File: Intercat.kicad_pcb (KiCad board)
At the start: 2 copper layers, 74.9 x 37.5 mm, 81 parts, among them J1 Conn_01x02, J2 Conn_01x02, J3 DE9_Receptacle, J4 USB_C_Receptacle_USB2.0, J5 Conn_01x02, T1 LM-NP-1001-B1L, T4 LM-NP-1001-B1L, U1 CP2615-xx-xM, U10 MAX3250, U11 EL357N(C)(TA)-G, U12 EL357N(C)(TA)-G, U2 USBLC6-2SC6, U3 PCM3060, U4 MCP6002, U6 MCP6002, U8 EL357N(C)(TA)-G, U9 EL357N(C)(TA)-G

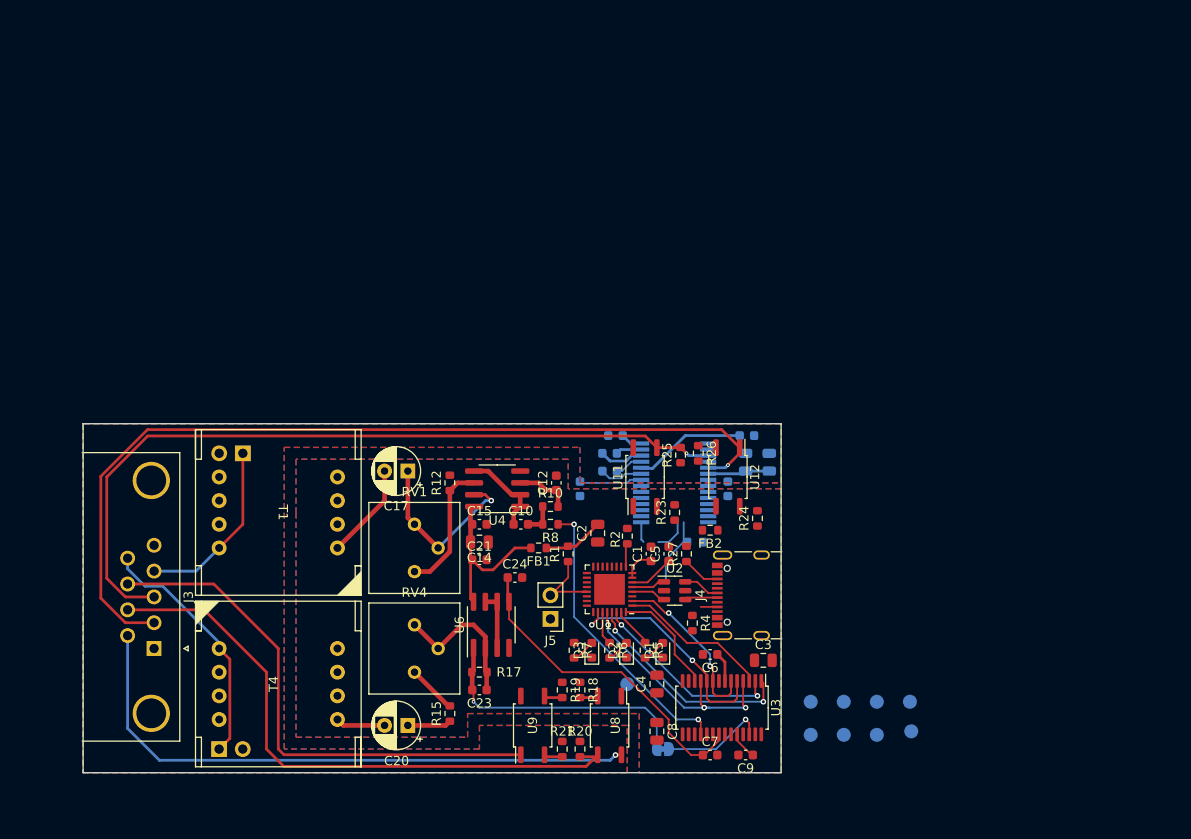
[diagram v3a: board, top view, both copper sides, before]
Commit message: redone layout, reduced size, added clearance for box
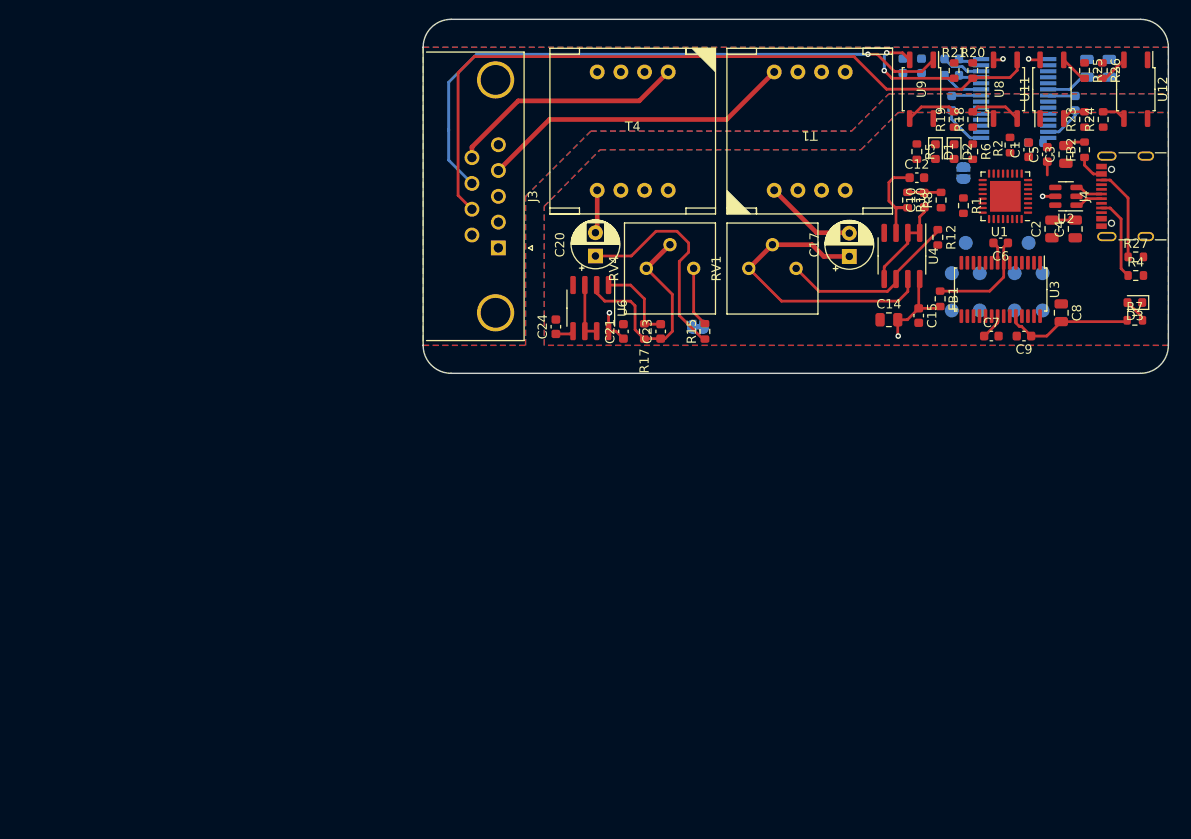
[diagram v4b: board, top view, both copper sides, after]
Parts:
- removed J1, J2, J5: Conn_01x02, Connector_PinHeader_2.54mm:PinHeader_1x02_P2.54mm_Vertical
- added JP1: Jumper_2_Open, Jumper:SolderJumper-2_P1.3mm_Open_RoundedPad1.0x1.5mm, B.Cu at (158.0, 78.5)
- added TP9: TestPoint, TestPoint:TestPoint_Pad_D1.5mm, B.Cu at (156.8, 93.2)
- moved R20 84.2 mm to (159.0, 67.5)
- moved R21 84.1 mm to (157.0, 67.5)
- moved U8 80.4 mm to (162.5, 69.5), turned to 90 degrees
- moved U9 80.0 mm to (153.5, 69.5), turned to -90 degrees
- moved R18 74.3 mm to (159.0, 72.8), turned to 90 degrees
- moved R19 74.3 mm to (157.0, 72.8), turned to 90 degrees
- moved T4 70.5 mm to (122.5, 74.0), turned to 0 degrees
- moved T1 70.2 mm to (141.5, 74.0), turned to 180 degrees
- moved R7 69.8 mm to (176.4, 94.3), turned to 0 degrees
- moved D3 69.2 mm to (176.4, 92.4), turned to 180 degrees
- moved C4 66.4 mm to (170.0, 84.5)
- moved R6 66.2 mm to (159.0, 76.2)
- moved D2 64.0 mm to (157.0, 76.2), turned to -90 degrees
- moved C3 63.3 mm to (169.0, 76.5), turned to 90 degrees
- moved C8 62.5 mm to (168.5, 93.5)
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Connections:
- U2 pad 1: /D- -> /D+
- U2 pad 3: /D+ -> /D-
- U2 pad 4: /D+ -> /D-
- U2 pad 6: /D- -> /D+
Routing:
- net /RX_ISO: track 96.0 -> 0.00 mm, vias 1 -> 0
- net /TX_ISO: track 84.1 -> 3.05 mm, vias 1 -> 0
- net VS: track 64.6 -> 2.33 mm, vias 1 -> 2
- net /DAC_Rout: track 31.3 -> 0.00 mm, vias 2 -> 0
- net /DAC_Vref: track 35.2 -> 4.73 mm
- net /LRCLK: track 26.9 -> 0.00 mm, vias 3 -> 0
- net /MCLK: track 24.8 -> 0.00 mm, vias 2 -> 0
- net /SCL: track 23.5 -> 0.00 mm, vias 2 -> 0
- net /SDA: track 21.0 -> 0.00 mm, vias 2 -> 0
- net Net-(JP2-A): track 29.6 -> 8.90 mm, vias 1 -> 0
- net Net-(C20-Pad1): track 4.69 -> 23.6 mm
- net /SCLK: track 18.5 -> 0.00 mm, vias 2 -> 0
- net /DIN: track 16.3 -> 0.00 mm
- net /OUT_ISO: track 19.2 -> 34.0 mm
- net /RTS_ISO: track 64.8 -> 79.4 mm
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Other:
- board size 74.9 x 37.5 mm -> 80 x 38 mm

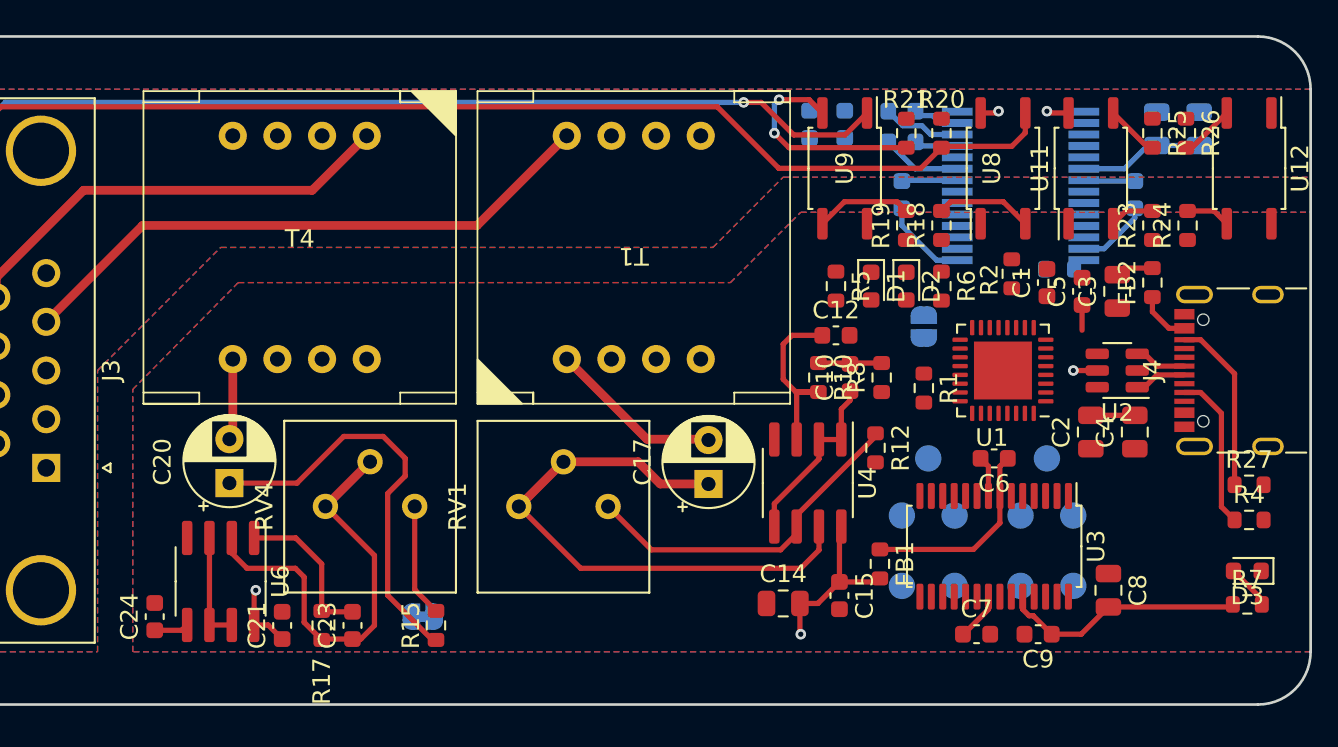
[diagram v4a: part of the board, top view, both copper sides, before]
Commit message: removed missed cap,reviewed layout
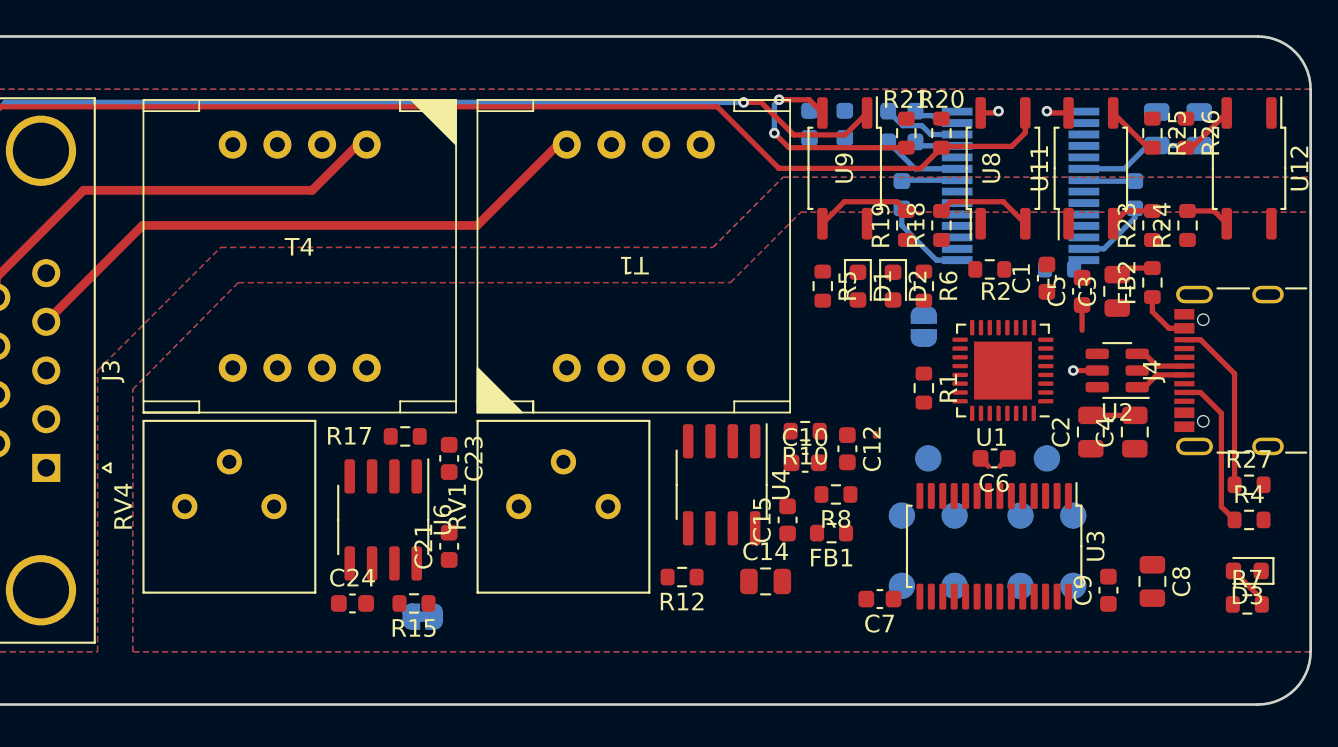
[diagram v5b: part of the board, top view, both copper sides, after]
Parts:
- removed C17, C20: C_Polarized, Capacitor_THT:CP_Radial_D5.0mm_P2.50mm
- R15: value 3k9 -> 9k1
- moved R12 13.2 mm to (144.2, 92.8), turned to 180 degrees
- moved R17 11.8 mm to (128.5, 84.8), turned to 0 degrees
- moved C24 11.3 mm to (125.5, 94.2), turned to 0 degrees
- moved C23 11.0 mm to (131.0, 86.0), turned to -90 degrees
- moved C21 10.5 mm to (131.0, 91.0)
- moved U6 9.89 mm to (127.2, 89.5)
- moved RV4 8.00 mm to (121.0, 88.7)
- moved R8 7.14 mm to (153.0, 88.0), turned to 180 degrees
- moved C12 6.48 mm to (153.7, 85.5), turned to -90 degrees
- moved C7 5.85 mm to (155.5, 94.0), turned to 180 degrees
- moved C10 5.48 mm to (151.2, 86.2), turned to 0 degrees
- moved C15 5.21 mm to (150.2, 89.5), turned to 90 degrees
- moved U4 4.90 mm to (146.5, 87.5)
- moved C9 4.72 mm to (168.5, 93.5), turned to 90 degrees
- moved FB1 3.26 mm to (152.8, 90.2), turned to 180 degrees
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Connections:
- R12 pad 2: GND -> /Analog Filter/Vref#
- R15 pad 1: Net-(C20-Pad1) -> /Analog Filter/Vref#
- RV1 pad 2: Net-(C17-Pad1) -> Net-(T1-AA)
- RV1 pad 3: Net-(C17-Pad1) -> Net-(T1-AA)
- T1 pad 4: GND -> /Analog Filter/Vref#
- T4 pad 5: Net-(T4-SA) -> /Analog Filter/Vref#
- T4 pad 8: GND -> Net-(T4-SB)
- U4 pad 7: Net-(C17-Pad1) -> Net-(T1-AA)
- U6 pad 3: /Analog Filter/Vref# -> Net-(T4-SB)
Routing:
- net Net-(C17-Pad1): track 32.7 -> 0.00 mm
- net Net-(U6A--): track 24.4 -> 0.00 mm
- net Net-(C20-Pad1): track 23.6 -> 0.00 mm
- net Net-(U4B--): track 19.7 -> 0.17 mm
- net VDDA: track 14.0 -> 0.00 mm, vias 2 -> 0
- net VBUS: track 17.6 -> 3.81 mm
- net VDD: track 15.2 -> 4.57 mm
- net Net-(U4A-+): track 10.7 -> 0.00 mm
- net Net-(U4A--): track 10.2 -> 0.00 mm
- net Net-(T1-AA): track 10.00 -> 0.00 mm
- net Net-(JP2-A): track 8.90 -> 0.00 mm
- net Net-(R15-Pad2): track 6.45 -> 0.00 mm
- net /Analog Filter/Vref#: track 6.22 -> 0.00 mm
- net /DAC_Vref: track 4.73 -> 0.00 mm
- net Net-(T4-SA): track 4.68 -> 0.00 mm
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
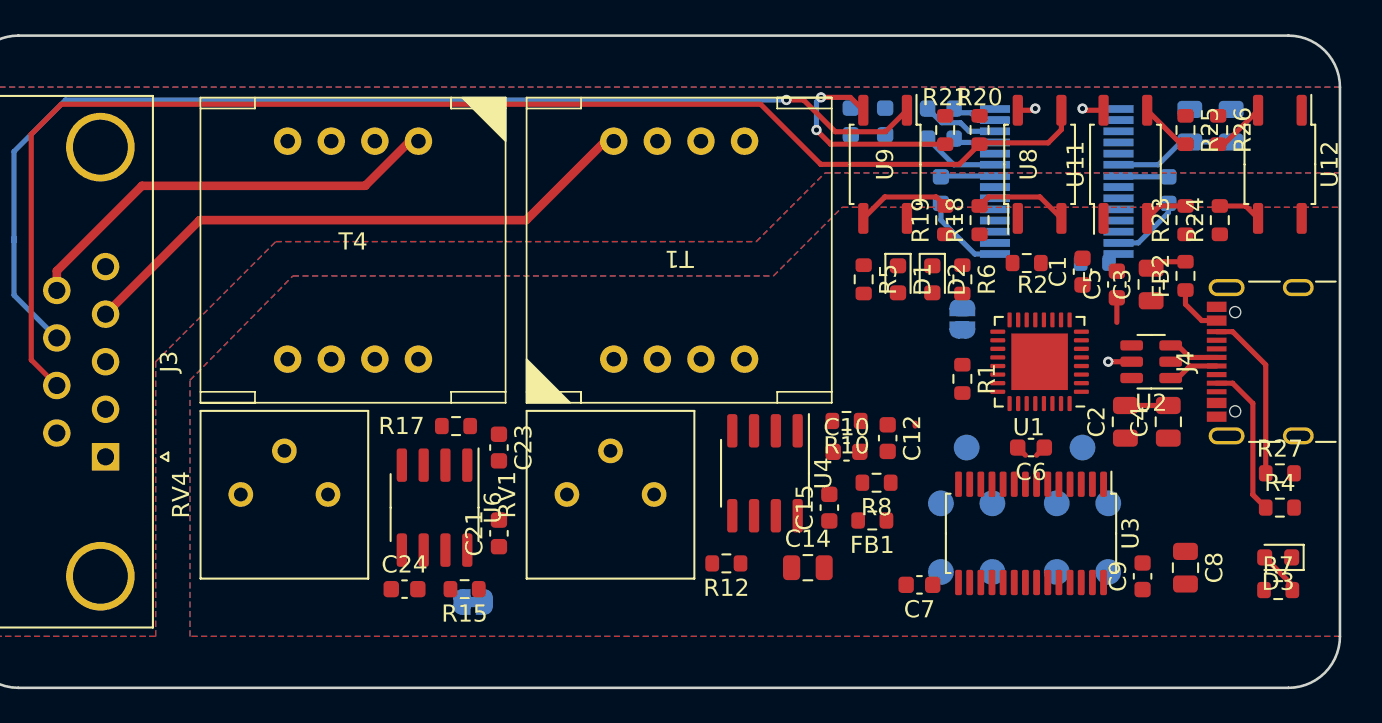
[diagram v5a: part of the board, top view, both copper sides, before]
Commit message: corrected gain of the amplifiers and dyn range, continued PCB
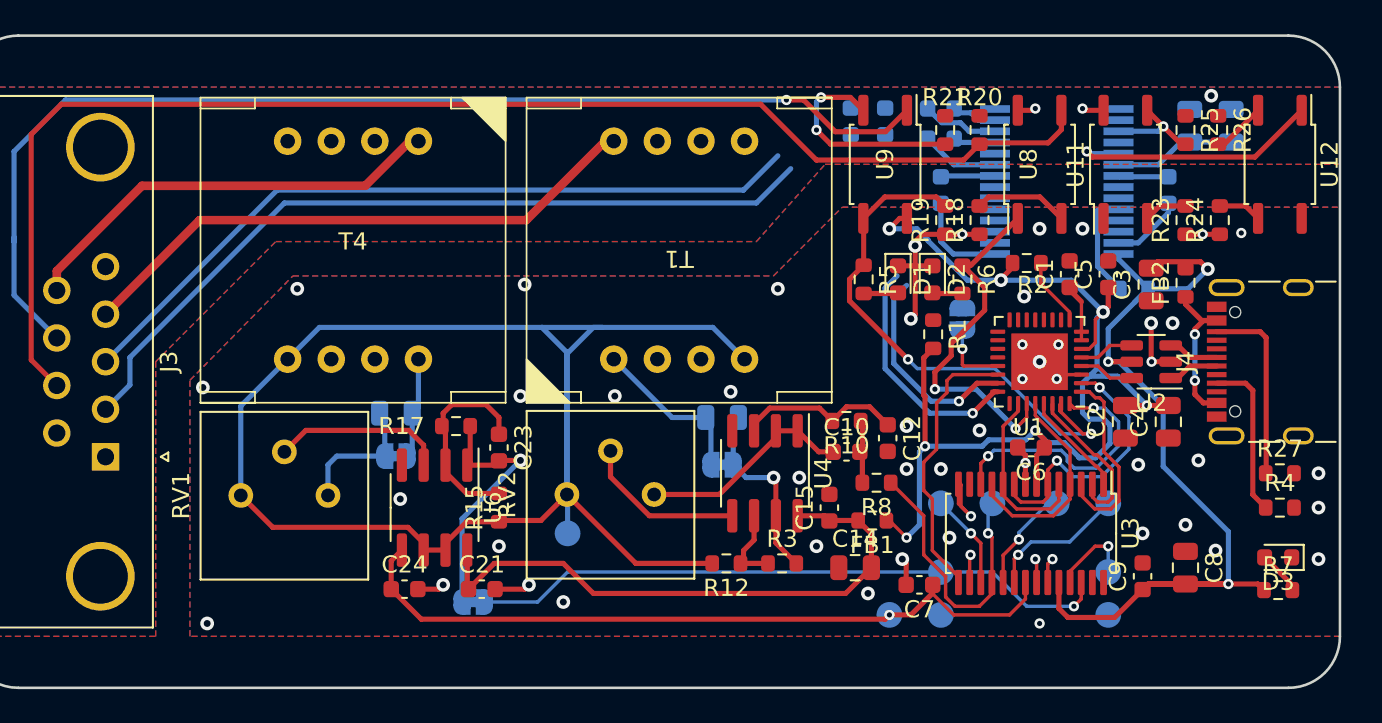
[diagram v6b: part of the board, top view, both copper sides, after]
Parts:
- removed RV4: 10k, Potentiometer_THT:Potentiometer_Bourns_3386P_Vertical
- added C11: 1u, Capacitor_SMD:C_0805_2012Metric, B.Cu at (125.0, 84.0)
- added C13: 1u, Capacitor_SMD:C_0805_2012Metric, B.Cu at (144.0, 84.2)
- added JP3: Jumper_2_Bridged, Jumper:SolderJumper-2_P1.3mm_Bridged_RoundedPad1.0x1.5mm, B.Cu at (125.0, 86.5)
- added JP4: Jumper_2_Bridged, Jumper:SolderJumper-2_P1.3mm_Bridged_RoundedPad1.0x1.5mm, B.Cu at (144.0, 87.0)
- added R3: 9k1, Resistor_SMD:R_0603_1608Metric, F.Cu at (147.5, 92.8)
- added RV2: 10k, Potentiometer_THT:Potentiometer_Bourns_3386P_Vertical, F.Cu at (140.0, 88.7)
- moved TP1 23.8 mm to (135.0, 91.0)
- moved RV1 19.0 mm to (121.0, 88.8)
- moved TP2 14.9 mm to (153.8, 95.8)
- moved R15 5.15 mm to (131.0, 89.5), turned to 90 degrees
- moved TP19 3.91 mm to (166.5, 95.8)
- moved C21 3.40 mm to (130.0, 94.2), turned to 0 degrees
- moved R1 3.11 mm to (156.3, 79.4)
- moved TP3 3.00 mm to (156.8, 93.2)
- moved C14 2.75 mm to (151.8, 93.0)
- moved R22 2.74 mm to (168.0, 76.8), turned to 180 degrees
- moved TP9 2.50 mm to (156.8, 95.8)
- moved C5 0.78 mm to (166.5, 75.9)
- moved C1 0.76 mm to (164.2, 75.9)
- moved FB2 0.40 mm to (171.0, 76.4)
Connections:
- R15 pad 2: Net-(R15-Pad2) -> Net-(U6A--)
- RV1 pad 1: Net-(U4B--) -> Net-(JP3-B)
- RV1 pad 2: Net-(T1-AA) -> Net-(U6A-+)
- RV1 pad 3: Net-(T1-AA) -> /Analog Filter/Vref#
- T1 pad 1: Net-(T1-AA) -> Net-(JP4-B)
- T4 pad 8: Net-(T4-SB) -> Net-(JP3-A)
- TP1 pad 1: Net-(U3-ZEROR) -> /Analog Filter/Vref#
- TP2 pad 1: Net-(U3-ZEROL) -> /DAC_Vref
- U3 pad 13: Net-(U3-ZEROR) -> unconnected-(U3-ZEROR-Pad13)
- U3 pad 14: Net-(U3-ZEROL) -> unconnected-(U3-ZEROL-Pad14)
- U4 pad 5: Net-(U4A--) -> Net-(U4B-+)
- U4 pad 7: Net-(T1-AA) -> Net-(JP4-A)
- U6 pad 3: Net-(T4-SB) -> Net-(U6A-+)
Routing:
- net /Analog Filter/Vref#: track 0.00 -> 93.0 mm
- net VDD: track 4.57 -> 68.3 mm, vias 0 -> 7
- net /RX_ISO: track 0.00 -> 62.3 mm, vias 0 -> 1
- net VBUS: track 3.81 -> 59.8 mm, vias 1 -> 3
- net /TX_ISO: track 3.05 -> 49.9 mm, vias 0 -> 1
- net /DAC_Vref: track 0.00 -> 43.7 mm, vias 0 -> 1
- net /ADC_Rin: track 0.00 -> 37.5 mm, vias 0 -> 1
- net VDDA: track 0.00 -> 34.5 mm
- net GND: track 1.70 -> 31.5 mm, vias 0 -> 51
- net /CTS: track 5.51 -> 31.3 mm, vias 0 -> 2
- net /RTS: track 0.00 -> 20.9 mm, vias 0 -> 2
- net /DAC_Rout: track 0.00 -> 16.7 mm, vias 0 -> 1
- net /RESET_OUT: track 0.00 -> 16.3 mm
- net /SCLK: track 0.00 -> 15.9 mm, vias 0 -> 2
- net /DOUT: track 0.00 -> 15.4 mm, vias 0 -> 2
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- added copper zone on B.Cu, net /Analog Filter/Vref#

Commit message: first PCB version
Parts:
- moved R1 2.01 mm to (158.3, 79.6), turned to 90 degrees
- moved C28 1.58 mm to (152.0, 68.5), turned to 180 degrees
- moved C29 1.51 mm to (152.0, 66.8), turned to 180 degrees
- moved C32 1.04 mm to (174.7, 67.2)
- moved R20 0.80 mm to (159.0, 66.7), turned to 90 degrees
- moved R21 0.80 mm to (157.0, 66.7), turned to 90 degrees
- moved JP1 0.73 mm to (158.2, 79.2)
- moved C27 0.15 mm to (171.4, 67.2)
- moved C31 0.15 mm to (156.8, 66.4)
- moved C30 0.10 mm to (156.8, 68.1)
- moved C7 0.10 mm to (155.4, 94.0)
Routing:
- net VS: track 2.33 -> 88.5 mm
- net /RX: track 14.8 -> 49.7 mm, vias 1 -> 2
- net /TX: track 13.8 -> 37.5 mm, vias 1 -> 2
- net /TX_ISO: track 49.9 -> 73.0 mm, vias 1 -> 2
- net VDD: track 68.3 -> 89.9 mm, vias 7 -> 8
- net /RX_ISO: track 62.3 -> 80.3 mm, vias 1 -> 2
- net Net-(U10-V+): track 0.00 -> 9.09 mm
- net Net-(U10-V-): track 0.00 -> 8.28 mm
- net /D+: track 6.19 -> 13.2 mm
- net Net-(R21-Pad2): track 12.6 -> 6.00 mm, vias 2 -> 0
- net /D-: track 6.19 -> 12.5 mm, vias 0 -> 2
- net GNDA: track 0.00 -> 5.69 mm, vias 1 -> 6
- net unconnected-(U3-ZEROL-Pad14): track 4.04 -> 0.00 mm, vias 1 -> 0
- net Net-(U10-nSHDN): track 6.36 -> 9.25 mm
- net /RTS: track 20.9 -> 23.4 mm
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- added copper zone on B.Cu, net VDD
